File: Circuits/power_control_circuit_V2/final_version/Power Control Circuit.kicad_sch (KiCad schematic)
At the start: 39 parts, among them Q10 IRF1405, Q12 IRF1405, Q23 S8050, Q24 S8550, Q3 S8050, Q4 IRF1405, Q4 S8550, Q8 IRF1405, Q9 IRF1405, U1 PC817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

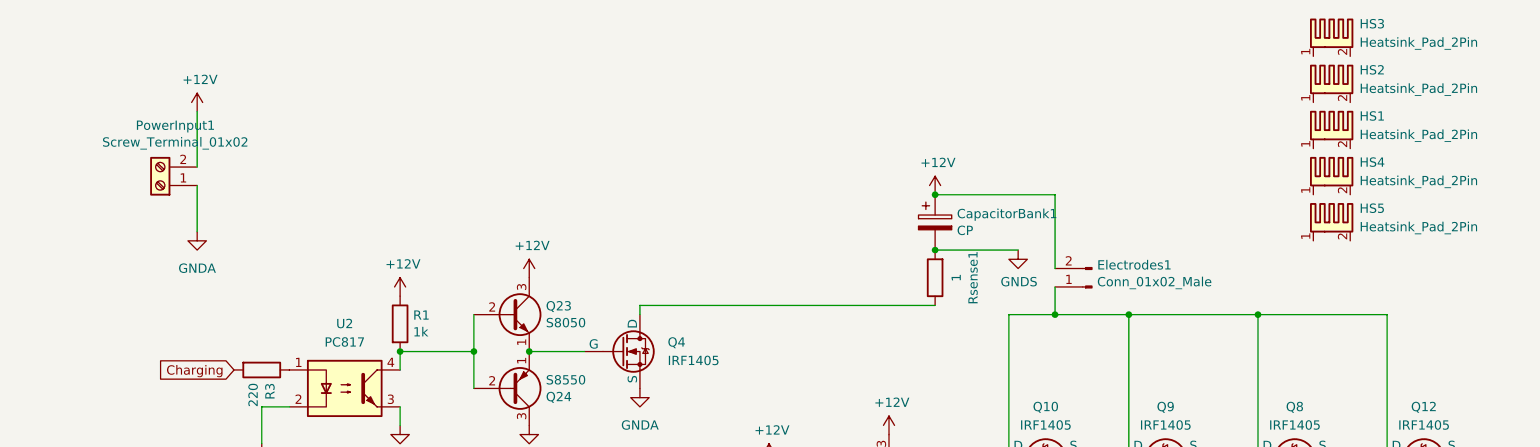
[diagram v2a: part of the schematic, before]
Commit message: started pad changes
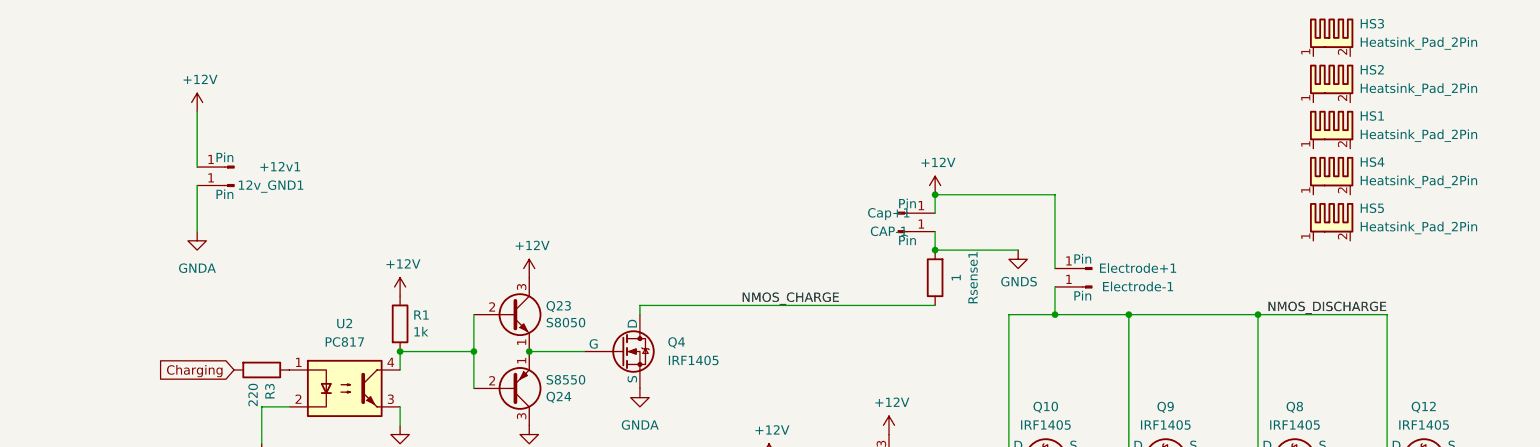
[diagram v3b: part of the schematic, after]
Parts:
- removed CapacitorBank1: CP, TerminalBlock:TerminalBlock_bornier-2_P5.08mm, symbol circuit-rescue:CP-Device
- removed Electrodes1: Conn_01x02_Male, TerminalBlock:TerminalBlock_bornier-2_P5.08mm, symbol circuit-rescue:Conn_01x02_Male-Connector
- removed PowerInput1: Screw_Terminal_01x02, TerminalBlock:TerminalBlock_bornier-2_P5.08mm, symbol Connector:Screw_Terminal_01x02
- added +12v1, 12v_GND1, CAP-1, Cap+1, Electrode+1, Electrode-1: Pin, MountingHole:MountingHole_4.3mm_M4_Pad, symbol Connector:Conn_01x01_Pin
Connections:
- net +12V: now also +12v1.1 (Pin_1), Cap+1.1 (Pin_1), Electrode+1.1 (Pin_1)
- net GNDA: now also 12v_GND1.1 (Pin_1)
- net GNDS: now also CAP-1.1 (Pin_1)
- net NMOS_DISCHARGE: now reaches Q10.1 (D), Q12.1 (D), Q8.1 (D), Q9.1 (D)
- net NMOS_DISCHARGE: now also Electrode-1.1 (Pin_1)
- net NMOS_CHARGE: now reaches Q4.1 (D), Rsense1.1
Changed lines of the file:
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@@
   (junction (at 186.69 53.34) (diameter 0) (color 0 0 0 0)
   )
+  (junction (at 142.24 44.45) (diameter 0) (color 0 0 0 0)
+  )
   (junction (at 186.69 87.63) (diameter 0) (color 0 0 0 0)
   )
-  (junction (at 142.24 44.45) (diameter 0) (color 0 0 0 0)
-  )
   (junction (at 119.38 81.28) (diameter 0) (color 0 0 0 0)
   )
@@
   (junction (at 179.07 87.63) (diameter 0) (color 0 0 0 0)
   )
+  (junction (at 191.77 80.01) (diameter 0) (color 0 0 0 0)
+  )
+  (junction (at 158.75 53.34) (diameter 0) (color 0 0 0 0)
+  )
+  (junction (at 86.36 58.42) (diameter 0) (color 0 0 0 0)
+  )
   (junction (at 142.24 36.83) (diameter 0) (color 0 0 0 0)
   )
-  (junction (at 191.77 80.01) (diameter 0) (color 0 0 0 0)
-  )
-  (junction (at 158.75 53.34) (diameter 0) (color 0 0 0 0)
-  )
-  (junction (at 86.36 58.42) (diameter 0) (color 0 0 0 0)
-  )
   (junction (at 128.27 81.28) (diameter 0) (color 0 0 0 0)
   )
@@
     (stroke (width 0) (type default))
   )
+  (wire (pts (xy 142.24 41.91) (xy 142.24 44.45))
+    (stroke (width 0) (type default))
+  )
   (wire (pts (xy 157.48 80.01) (xy 173.99 80.01))
     (stroke (width 0) (type default))
@@
     (stroke (width 0) (type default))
   )
+  (wire (pts (xy 142.24 36.83) (xy 142.24 39.37))
+    (stroke (width 0) (type default))
+  )
   (wire (pts (xy 186.69 72.39) (xy 186.69 53.34))
     (stroke (width 0) (type default))
@@
   (wire (pts (xy 101.6 91.44) (xy 101.6 88.9))
     (stroke (width 0) (type default))
+  )
+  (label "NMOS_DISCHARGE" (at 187.96 53.34 0) (fields_autoplaced)
+    (effects (font (size 1.27 1.27)) (justify left bottom))
+  )
+  (label "NMOS_CHARGE" (at 115.57 52.07 0) (fields_autoplaced)
+    (effects (font (size 1.27 1.27)) (justify left bottom))
   )
   (global_label "Discharge" (shape input) (at 96.52 83.82 180)
@@
     )
   )
-  (symbol (lib_id "Connector:Screw_Terminal_01x02") (at 35.56 35.56 180) (unit 1)
-    (in_bom yes) (on_board yes) (dnp no)
-    (property "Reference" "PowerInput1" (at 37.6428 27.305 0)
-      (effects (font (size 1.27 1.27)))
-    )
-    (property "Value" "Screw_Terminal_01x02" (at 37.6428 29.6164 0)
-      (effects (font (size 1.27 1.27)))
-    )
-    (property "Footprint" "TerminalBlock:TerminalBlock_bornier-2_P5.08mm" (at 35.56 35.56 0)
-      (effects (font (size 1.27 1.27)) hide)
-    )
-    (property "Datasheet" "~" (at 35.56 35.56 0)
-      (effects (font (size 1.27 1.27)) hide)
-    )
-    (pin "1")
-    (pin "2")
-    (instances
-      (project "circuit"
-        (path "/f264ea13-7799-4257-b194-79457d1fa1ab"
-          (reference "PowerInput1") (unit 1)
-        )
-      )
-      (project "Power Control Circuit"
-        (path "/f5e3c383-3430-4217-817e-2eedfeb82870"
-          (reference "PowerInput1") (unit 1)
+  (symbol (lib_id "Connector:Conn_01x01_Pin") (at 137.16 39.37 0) (unit 1)
+    (in_bom yes) (on_board yes) (dnp no)
+    (property "Reference" "Cap+1" (at 135.89 39.37 0)
+      (effects (font (size 1.27 1.27)))
+    )
+    (property "Value" "Pin" (at 138.43 38.1 0)
+      (effects (font (size 1.27 1.27)))
+    )
+    (property "Footprint" "MountingHole:MountingHole_4.3mm_M4_Pad" (at 137.16 39.37 0)
+      (effects (font (size 1.27 1.27)) hide)
+    )
+    (property "Datasheet" "~" (at 137.16 39.37 0)
+      (effects (font (size 1.27 1.27)) hide)
+    )
+    (pin "1")
+    (instances
+      (project "Power Control Circuit"
+        (path "/f5e3c383-3430-4217-817e-2eedfeb82870"
+          (reference "Cap+1") (unit 1)
         )
       )
@@
     )
   )
+  (symbol (lib_id "Connector:Conn_01x01_Pin") (at 163.83 46.99 180) (unit 1)
+    (in_bom yes) (on_board yes) (dnp no)
+    (property "Reference" "Electrode+1" (at 170.18 46.99 0)
+      (effects (font (size 1.27 1.27)))
+    )
+    (property "Value" "Pin" (at 162.56 45.72 0)
+      (effects (font (size 1.27 1.27)))
+    )
+    (property "Footprint" "MountingHole:MountingHole_4.3mm_M4_Pad" (at 163.83 46.99 0)
+      (effects (font (size 1.27 1.27)) hide)
+    )
+    (property "Datasheet" "~" (at 163.83 46.99 0)
+      (effects (font (size 1.27 1.27)) hide)
+    )
+    (pin "1")
+    (instances
+      (project "Power Control Circuit"
+        (path "/f5e3c383-3430-4217-817e-2eedfeb82870"
+          (reference "Electrode+1") (unit 1)
+        )
+      )
+    )
+  )
   (symbol (lib_id "power:GNDA") (at 135.89 90.17 0) (unit 1)
     (in_bom yes) (on_board yes) (dnp no) (fields_autoplaced)
@@
     )
   )
-  (symbol (lib_id "circuit-rescue:Conn_01x02_Male-Connector") (at 163.83 49.53 180) (unit 1)
-    (in_bom yes) (on_board yes) (dnp no)
-    (property "Reference" "Electrodes1" (at 164.5412 46.5328 0)
-      (effects (font (size 1.27 1.27)) (justify right))
-    )
-    (property "Value" "Conn_01x02_Male" (at 164.5412 48.8442 0)
-      (effects (font (size 1.27 1.27)) (justify right))
-    )
-    (property "Footprint" "TerminalBlock:TerminalBlock_bornier-2_P5.08mm" (at 163.83 49.53 0)
-      (effects (font (size 1.27 1.27)) hide)
-    )
-    (property "Datasheet" "~" (at 163.83 49.53 0)
-      (effects (font (size 1.27 1.27)) hide)
-    )
-    (pin "1")
-    (pin "2")
-    (instances
-      (project "circuit"
-        (path "/f264ea13-7799-4257-b194-79457d1fa1ab"
-          (reference "Electrodes1") (unit 1)
-        )
-      )
-      (project "Power Control Circuit"
-        (path "/f5e3c383-3430-4217-817e-2eedfeb82870"
-          (reference "Electrodes1") (unit 1)
-        )
-      )
-    )
-  )
-  (symbol (lib_id "circuit-rescue:CP-Device") (at 142.24 40.64 0) (unit 1)
-    (in_bom yes) (on_board yes) (dnp no)
-    (property "Reference" "CapacitorBank1" (at 145.2372 39.4716 0)
-      (effects (font (size 1.27 1.27)) (justify left))
-    )
-    (property "Value" "CP" (at 145.2372 41.783 0)
-      (effects (font (size 1.27 1.27)) (justify left))
-    )
-    (property "Footprint" "TerminalBlock:TerminalBlock_bornier-2_P5.08mm" (at 143.2052 44.45 0)
-      (effects (font (size 1.27 1.27)) hide)
-    )
-    (property "Datasheet" "~" (at 142.24 40.64 0)
-      (effects (font (size 1.27 1.27)) hide)
-    )
-    (pin "1")
-    (pin "2")
-    (instances
-      (project "circuit"
-        (path "/f264ea13-7799-4257-b194-79457d1fa1ab"
-          (reference "CapacitorBank1") (unit 1)
-        )
-      )
-      (project "Power Control Circuit"
-        (path "/f5e3c383-3430-4217-817e-2eedfeb82870"
-          (reference "CapacitorBank1") (unit 1)
-        )
-      )
-    )
-  )
   (symbol (lib_id "power:+12V") (at 119.38 73.66 0) (unit 1)
     (in_bom yes) (on_board yes) (dnp no)
@@
         (path "/f5e3c383-3430-4217-817e-2eedfeb82870"
           (reference "Rsense1") (unit 1)
+        )
+      )
+    )
+  )
+  (symbol (lib_id "Connector:Conn_01x01_Pin") (at 163.83 49.53 180) (unit 1)
+    (in_bom yes) (on_board yes) (dnp no)
+    (property "Reference" "Electrode-1" (at 170.18 49.53 0)
+      (effects (font (size 1.27 1.27)))
+    )
+    (property "Value" "Pin" (at 162.56 50.8 0)
+      (effects (font (size 1.27 1.27)))
+    )
+    (property "Footprint" "MountingHole:MountingHole_4.3mm_M4_Pad" (at 163.83 49.53 0)
+      (effects (font (size 1.27 1.27)) hide)
+    )
+    (property "Datasheet" "~" (at 163.83 49.53 0)
+      (effects (font (size 1.27 1.27)) hide)
+    )
+    (pin "1")
+    (instances
+      (project "Power Control Circuit"
+        (path "/f5e3c383-3430-4217-817e-2eedfeb82870"
+          (reference "Electrode-1") (unit 1)
         )
       )
@@
     )
   )
+  (symbol (lib_id "Connector:Conn_01x01_Pin") (at 45.72 35.56 180) (unit 1)
+    (in_bom yes) (on_board yes) (dnp no)
+    (property "Reference" "12v_GND1" (at 50.8 35.56 0)
+      (effects (font (size 1.27 1.27)))
+    )
+    (property "Value" "Pin" (at 44.45 36.83 0)
+      (effects (font (size 1.27 1.27)))
+    )
+    (property "Footprint" "MountingHole:MountingHole_4.3mm_M4_Pad" (at 45.72 35.56 0)
+      (effects (font (size 1.27 1.27)) hide)
+    )
+    (property "Datasheet" "~" (at 45.72 35.56 0)
+      (effects (font (size 1.27 1.27)) hide)
+    )
+    (pin "1")
+    (instances
+      (project "Power Control Circuit"
+        (path "/f5e3c383-3430-4217-817e-2eedfeb82870"
+          (reference "12v_GND1") (unit 1)
+        )
+      )
+    )
+  )
   (symbol (lib_id "Simulation_SPICE:NMOS") (at 99.06 58.42 0) (unit 1)
     (in_bom yes) (on_board yes) (dnp no) (fields_autoplaced)
@@
         )
       )
+    )
+  )
+  (symbol (lib_id "Connector:Conn_01x01_Pin") (at 45.72 33.02 180) (unit 1)
+    (in_bom yes) (on_board yes) (dnp no)
+    (property "Reference" "+12v1" (at 52.07 33.02 0)
+      (effects (font (size 1.27 1.27)))
+    )
+    (property "Value" "Pin" (at 44.45 31.75 0)
+      (effects (font (size 1.27 1.27)))
+    )
+    (property "Footprint" "MountingHole:MountingHole_4.3mm_M4_Pad" (at 45.72 33.02 0)
+      (effects (font (size 1.27 1.27)) hide)
+    )
+    (property "Datasheet" "~" (at 45.72 33.02 0)
+      (effects (font (size 1.27 1.27)) hide)
+    )
+    (pin "1")
+    (instances
+      (project "Power Control Circuit"
+        (path "/f5e3c383-3430-4217-817e-2eedfeb82870"
+          (reference "+12v1") (unit 1)
+        )
+      )
+    )
+  )
+  (symbol (lib_id "Connector:Conn_01x01_Pin") (at 137.16 41.91 0) (unit 1)
+    (in_bom yes) (on_board yes) (dnp no)
+    (property "Reference" "CAP-1" (at 135.89 41.91 0)
+      (effects (font (size 1.27 1.27)))
+    )
+    (property "Value" "Pin" (at 138.43 43.18 0)
+      (effects (font (size 1.27 1.27)))
+    )
+    (property "Footprint" "MountingHole:MountingHole_4.3mm_M4_Pad" (at 137.16 41.91 0)
+      (effects (font (size 1.27 1.27)) hide)
+    )
+    (property "Datasheet" "~" (at 137.16 41.91 0)
+      (effects (font (size 1.27 1.27)) hide)
+    )
+    (pin "1")
+    (instances
+      (project "Power Control Circuit"
+        (path "/f5e3c383-3430-4217-817e-2eedfeb82870"
+          (reference "CAP-1") (unit 1)
+        )
+      )

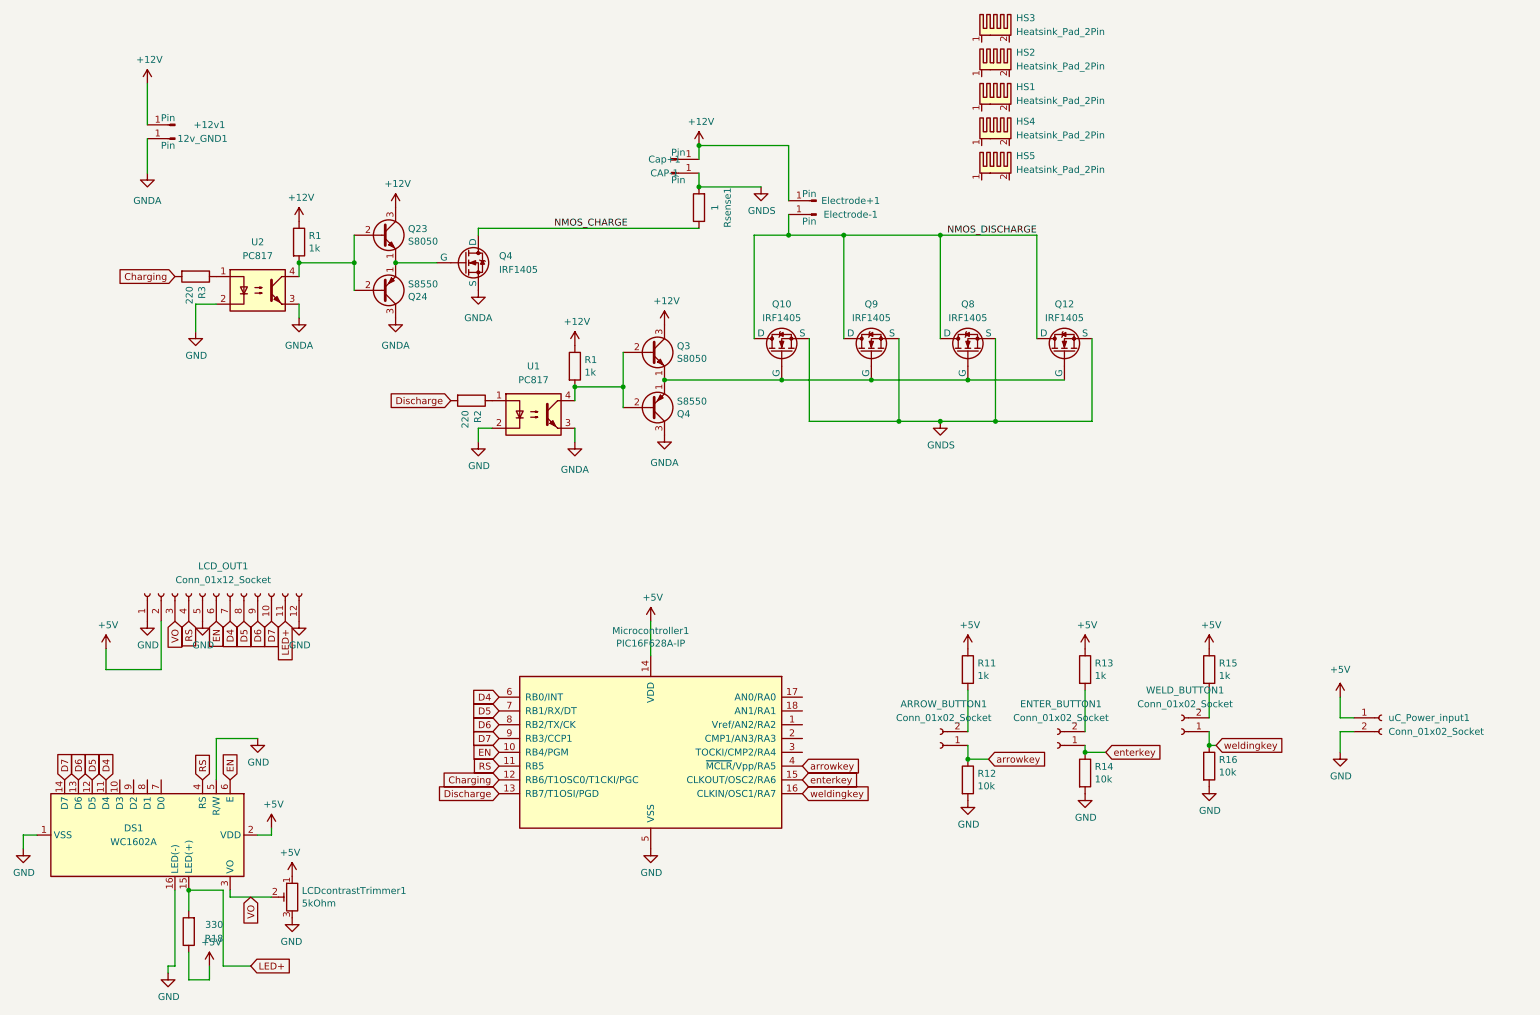
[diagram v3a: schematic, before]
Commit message: added terminal pads to the pcb
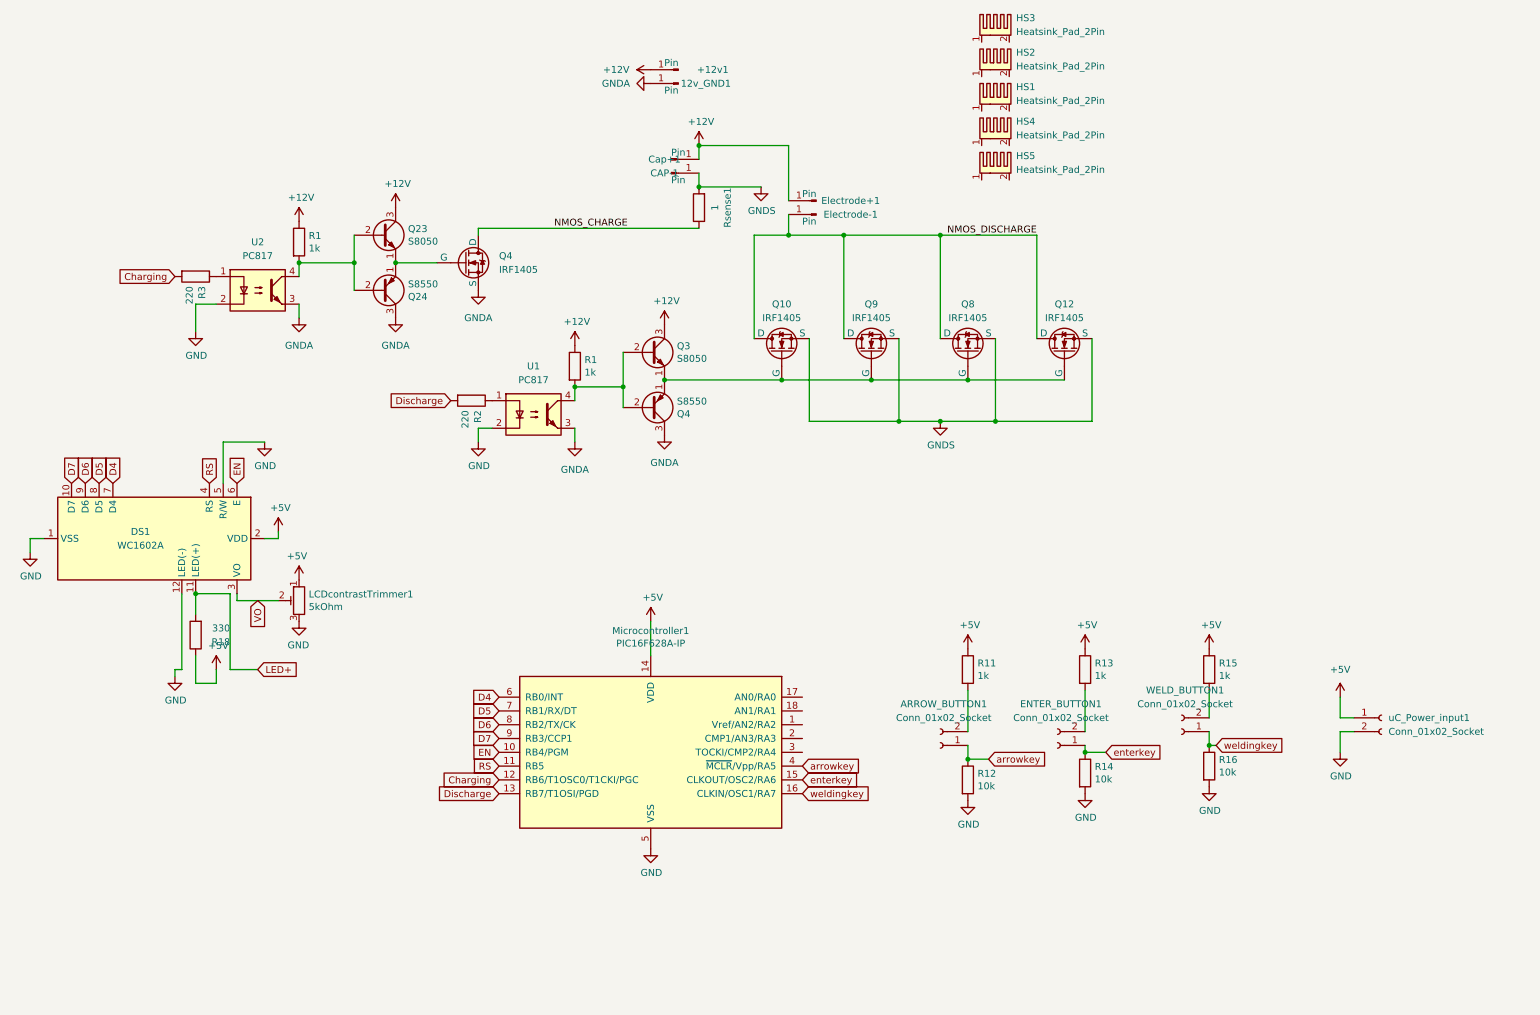
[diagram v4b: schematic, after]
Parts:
- removed LCD_OUT1: Conn_01x12_Socket, Connector_PinHeader_2.54mm:PinHeader_1x12_P2.54mm_Vertical, symbol Connector:Conn_01x12_Socket
- DS1: footprint Display:WC1602A -> Connector_PinSocket_2.54mm:PinSocket_1x12_P2.54mm_Vertical
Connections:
- net D4: now also DS1.7 (D4); no longer DS1.11 (D4)
- net D5: now also DS1.8 (D5); no longer DS1.12 (D5)
- net D6: now also DS1.9 (D6); no longer DS1.13 (D6)
- net D7: now also DS1.10 (D7); no longer DS1.14 (D7)
- net GND: now also DS1.12 (LED(-)); no longer DS1.16 (LED(-))
- net LED+: now also DS1.11 (LED(+)); no longer DS1.15 (LED(+))
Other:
- moved on the sheet: +12v1, 12v_GND1, LCDcontrastTrimmer1, R18

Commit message: redesigning the circuit
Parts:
- removed HS1, HS2, HS3, HS4, HS5: Heatsink_Pad_2Pin, Heatsink:Heatsink_Stonecold_HS-S03_13.21x12.7mm, symbol Mechanical:Heatsink_Pad_2Pin
- ARROW1: renamed from ARROW_BUTTON1; value Conn_01x02_Socket -> JST-2P
- ENTER1: renamed from ENTER_BUTTON1; value Conn_01x02_Socket -> JST-2P
- LCDcontrastTrimmer1: footprint Potentiometer_THT:Potentiometer_Bourns_3386C_Horizontal -> Connector_PinSocket_2.54mm:PinSocket_1x03_P2.54mm_Vertical
- Power5v1: renamed from uC_Power_input1; value Conn_01x02_Socket -> JST-2P
- WELD1: renamed from WELD_BUTTON1; value Conn_01x02_Socket -> JST-2P
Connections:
- net LED+: no longer names the net of DS1.11 (LED(+)), R18.2
- net VO: no longer names the net of DS1.3 (VO), LCDcontrastTrimmer1.2
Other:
- moved on the sheet: Power5v1, R18

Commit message: finished PCB (again)
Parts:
- added Bridge1: 0ohm, Resistor_THT:R_Axial_DIN0207_L6.3mm_D2.5mm_P5.08mm_Vertical, symbol Device:R
- added C1: 220uF, Capacitor_THT:CP_Radial_D6.3mm_P2.50mm, symbol Device:C_Polarized
- added H1, H2, H3: MountingHole, MountingHole:MountingHole_3.2mm_M3_DIN965_Pad_TopBottom, symbol Mechanical:MountingHole
- Q23, Q24, Q3, Q4: footprint Package_TO_SOT_THT:TO-92_Inline -> Package_TO_SOT_THT:TO-92_Inline_Wide
- R18: footprint Resistor_THT:R_Axial_DIN0207_L6.3mm_D2.5mm_P7.62mm_Horizontal -> Resistor_THT:R_Axial_DIN0309_L9.0mm_D3.2mm_P12.70mm_Horizontal
- Rsense1: value 1 -> 2ohm
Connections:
- net +5V: now also C1.1
- net GND: now also Bridge1.1, Bridge1.2, C1.2
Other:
- moved on the sheet: +12v1, 12v_GND1, CAP-1, Cap+1, DS1, Electrode+1, Electrode-1, LCDcontrastTrimmer1, Microcontroller1, Power5v1, Q10, Q12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

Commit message: minor changes
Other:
- moved on the sheet: +12v1, 12v_GND1, ARROW1, Bridge1, C1, CAP-1, Cap+1, DS1, ENTER1, Electrode+1, Electrode-1, H1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
